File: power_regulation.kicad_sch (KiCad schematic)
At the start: 5 parts, among them U1 NCP1117LPST33T3G

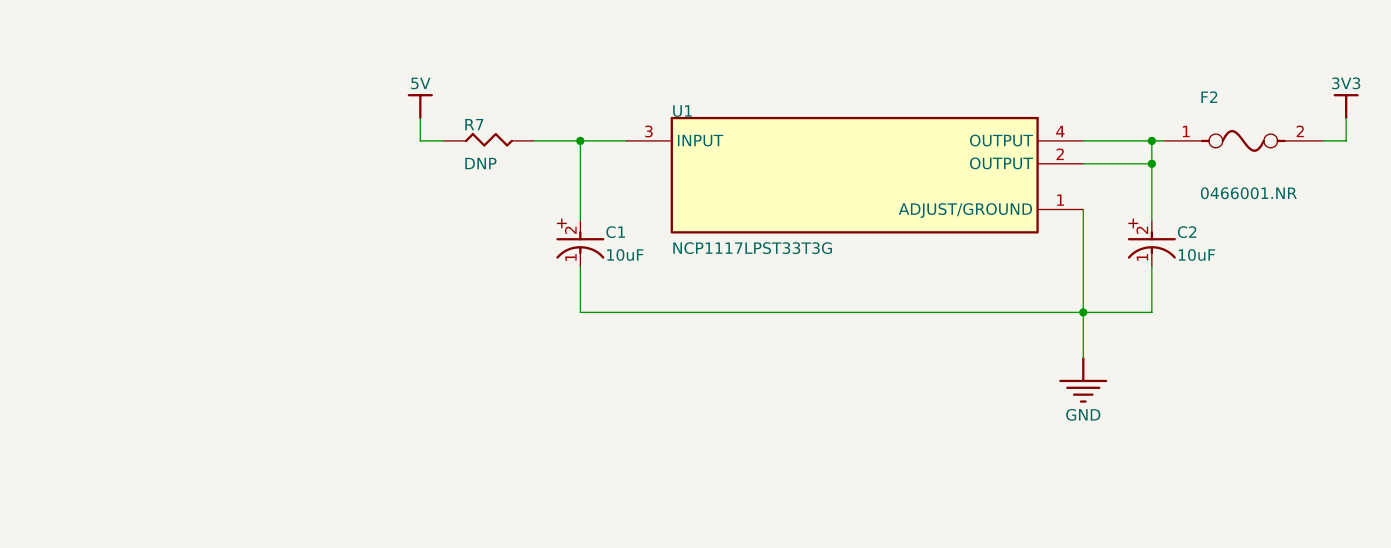
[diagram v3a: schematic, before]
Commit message: updated power and ground symbols in schematic to kicad library version
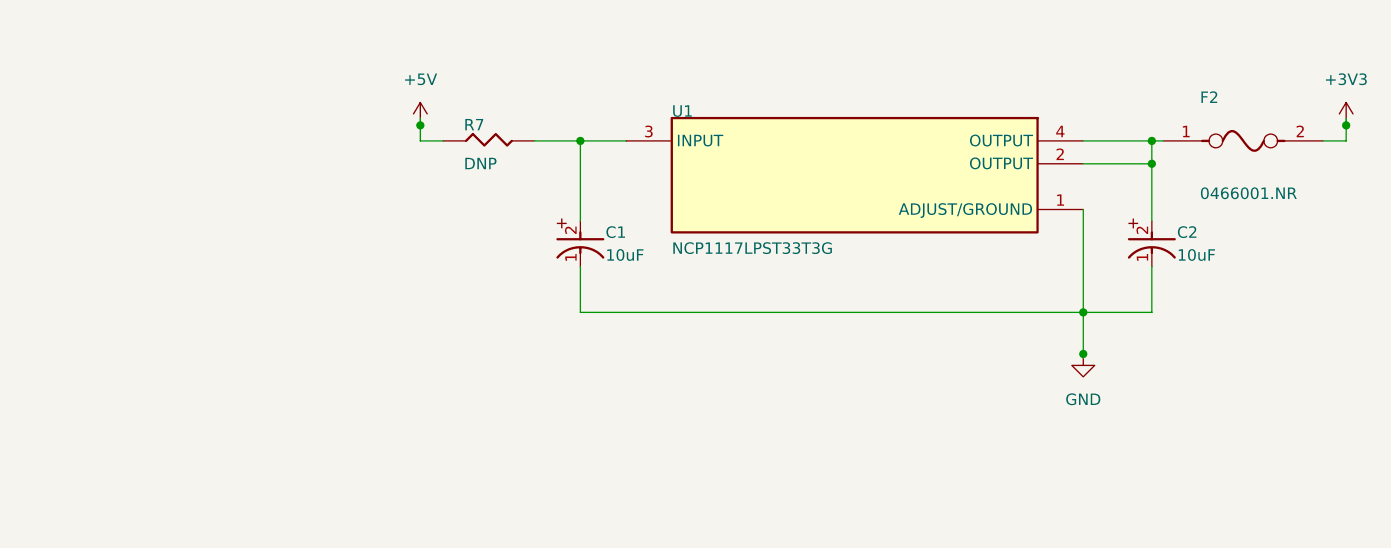
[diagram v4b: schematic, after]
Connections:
- net 3V3 renamed +3V3
- net 5V renamed +5V
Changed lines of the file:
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@@
 (kicad_sch (version 20230121) (generator eeschema)
   (paper "A4")
+  (junction (at 232.41 96.52) (diameter 0) (color 0 0 0 0)
+  )
+  (junction (at 203.2 121.92) (diameter 0) (color 0 0 0 0)
+  )
   (junction (at 203.2 117.2972) (diameter 0) (color 0 0 0 0)
   )
@@
   (junction (at 147.32 98.2472) (diameter 0) (color 0 0 0 0)
   )
+  (junction (at 129.54 96.52) (diameter 0) (color 0 0 0 0)
+  )
   (wire (pts (xy 147.32 98.2472) (xy 152.4 98.2472))
     (stroke (width 0.254) (type default))
@@
     (stroke (width 0.254) (type default))
   )
+  (wire (pts (xy 129.54 96.52) (xy 129.54 95.7072))
+    (stroke (width 0.254) (type default))
+  )
+  (wire (pts (xy 203.2 121.92) (xy 203.2 122.3772))
+    (stroke (width 0.254) (type default))
+  )
   (wire (pts (xy 210.82 100.7872) (xy 203.2 100.7872))
     (stroke (width 0.254) (type default))
@@
     (stroke (width 0.254) (type default))
   )
-  (wire (pts (xy 203.2 117.2972) (xy 203.2 122.3772))
+  (wire (pts (xy 203.2 117.2972) (xy 203.2 121.92))
     (stroke (width 0.254) (type default))
   )
@@
     (stroke (width 0.254) (type default))
   )
-  (wire (pts (xy 129.54 98.2472) (xy 129.54 95.7072))
+  (wire (pts (xy 129.54 98.2472) (xy 129.54 96.52))
     (stroke (width 0.254) (type default))
   )
@@
     (stroke (width 0.254) (type default))
   )
+  (wire (pts (xy 232.41 96.52) (xy 232.41 98.2472))
+    (stroke (width 0.254) (type default))
+  )
   (wire (pts (xy 147.32 98.2472) (xy 147.32 107.1372))
     (stroke (width 0.254) (type default))
@@
     (stroke (width 0.254) (type default))
   )
-  (wire (pts (xy 232.41 95.7072) (xy 232.41 98.2472))
+  (wire (pts (xy 232.41 95.7072) (xy 232.41 96.52))
     (stroke (width 0.254) (type default))
   )
@@
     )
   )
-  (symbol (lib_id "MEB-altium-import:3V3") (at 232.41 95.7072 180) (unit 1)
-    (in_bom yes) (on_board yes) (dnp no)
-    (property "Reference" "#PWR0132" (at 232.41 95.7072 0)
-      (effects (font (size 1.27 1.27)) hide)
-    )
-    (property "Value" "3V3" (at 232.41 91.8972 0)
+  (symbol (lib_id "power:+5V") (at 129.54 96.52 0) (unit 1)
+    (in_bom yes) (on_board yes) (dnp no) (fields_autoplaced)
+    (property "Reference" "#PWR028" (at 129.54 100.33 0)
+      (effects (font (size 1.27 1.27)) hide)
+    )
+    (property "Value" "+5V" (at 129.54 91.44 0)
       (effects (font (size 1.27 1.27)))
     )
-    (property "Footprint" "" (at 232.41 95.7072 0)
-      (effects (font (size 1.27 1.27)) hide)
-    )
-    (property "Datasheet" "" (at 232.41 95.7072 0)
-      (effects (font (size 1.27 1.27)) hide)
-    )
-    (pin "")
-    (instances
-      (project "MEB"
-        (path "/228e4997-23c1-4c21-939b-583cad26a5e3/90a8e139-216e-4b02-83ea-4edb1f5f4c15"
-          (reference "#PWR0132") (unit 1)
-        )
-      )
-    )
-  )
-  (symbol (lib_id "MEB-altium-import:5V") (at 129.54 95.7072 180) (unit 1)
-    (in_bom yes) (on_board yes) (dnp no)
-    (property "Reference" "#PWR0128" (at 129.54 95.7072 0)
-      (effects (font (size 1.27 1.27)) hide)
-    )
-    (property "Value" "5V" (at 129.54 91.8972 0)
+    (property "Footprint" "" (at 129.54 96.52 0)
+      (effects (font (size 1.27 1.27)) hide)
+    )
+    (property "Datasheet" "" (at 129.54 96.52 0)
+      (effects (font (size 1.27 1.27)) hide)
+    )
+    (pin "1")
+    (instances
+      (project "MEB"
+        (path "/228e4997-23c1-4c21-939b-583cad26a5e3"
+          (reference "#PWR028") (unit 1)
+        )
+        (path "/228e4997-23c1-4c21-939b-583cad26a5e3/90a8e139-216e-4b02-83ea-4edb1f5f4c15"
+          (reference "#PWR043") (unit 1)
+        )
+      )
+    )
+  )
+  (symbol (lib_id "power:GND") (at 203.2 121.92 0) (unit 1)
+    (in_bom yes) (on_board yes) (dnp no) (fields_autoplaced)
+    (property "Reference" "#PWR030" (at 203.2 128.27 0)
+      (effects (font (size 1.27 1.27)) hide)
+    )
+    (property "Value" "GND" (at 203.2 127 0)
       (effects (font (size 1.27 1.27)))
     )
-    (property "Footprint" "" (at 129.54 95.7072 0)
-      (effects (font (size 1.27 1.27)) hide)
-    )
-    (property "Datasheet" "" (at 129.54 95.7072 0)
-      (effects (font (size 1.27 1.27)) hide)
-    )
-    (pin "")
-    (instances
-      (project "MEB"
-        (path "/228e4997-23c1-4c21-939b-583cad26a5e3/90a8e139-216e-4b02-83ea-4edb1f5f4c15"
-          (reference "#PWR0128") (unit 1)
+    (property "Footprint" "" (at 203.2 121.92 0)
+      (effects (font (size 1.27 1.27)) hide)
+    )
+    (property "Datasheet" "" (at 203.2 121.92 0)
+      (effects (font (size 1.27 1.27)) hide)
+    )
+    (pin "1")
+    (instances
+      (project "MEB"
+        (path "/228e4997-23c1-4c21-939b-583cad26a5e3/3aab6a70-cc66-4393-a750-92acad576aaa"
+          (reference "#PWR030") (unit 1)
+        )
+        (path "/228e4997-23c1-4c21-939b-583cad26a5e3/90a8e139-216e-4b02-83ea-4edb1f5f4c15"
+          (reference "#PWR033") (unit 1)
         )
       )
@@
     )
   )
-  (symbol (lib_id "MEB-altium-import:GND") (at 203.2 122.3772 0) (unit 1)
-    (in_bom yes) (on_board yes) (dnp no)
-    (property "Reference" "#PWR0131" (at 203.2 122.3772 0)
-      (effects (font (size 1.27 1.27)) hide)
-    )
-    (property "Value" "GND" (at 203.2 128.7272 0)
+  (symbol (lib_id "power:+3V3") (at 232.41 96.52 0) (unit 1)
+    (in_bom yes) (on_board yes) (dnp no) (fields_autoplaced)
+    (property "Reference" "#PWR036" (at 232.41 100.33 0)
+      (effects (font (size 1.27 1.27)) hide)
+    )
+    (property "Value" "+3V3" (at 232.41 91.44 0)
       (effects (font (size 1.27 1.27)))
     )
-    (property "Footprint" "" (at 203.2 122.3772 0)
-      (effects (font (size 1.27 1.27)) hide)
-    )
-    (property "Datasheet" "" (at 203.2 122.3772 0)
-      (effects (font (size 1.27 1.27)) hide)
-    )
-    (pin "")
-    (instances
-      (project "MEB"
-        (path "/228e4997-23c1-4c21-939b-583cad26a5e3/90a8e139-216e-4b02-83ea-4edb1f5f4c15"
-          (reference "#PWR0131") (unit 1)
-        )
-      )
+    (property "Footprint" "" (at 232.41 96.52 0)
+      (effects (font (size 1.27 1.27)) hide)
+    )
+    (property "Datasheet" "" (at 232.41 96.52 0)
+      (effects (font (size 1.27 1.27)) hide)
+    )
+    (pin "1")
+    (instances
+      (project "MEB"
+        (path "/228e4997-23c1-4c21-939b-583cad26a5e3"
+          (reference "#PWR036") (unit 1)
+        )
+        (path "/228e4997-23c1-4c21-939b-583cad26a5e3/90a8e139-216e-4b02-83ea-4edb1f5f4c15"
+          (reference "#PWR040") (unit 1)
+        )
+      )

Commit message: Fix a variety of small issues
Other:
- moved on the sheet: C1, C2, F2, R7, U1
